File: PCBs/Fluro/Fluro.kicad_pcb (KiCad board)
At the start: 2 copper layers, 7 parts, among them J1 Conn_01x01_Pin, U1 OPT101P, U2 LM393N

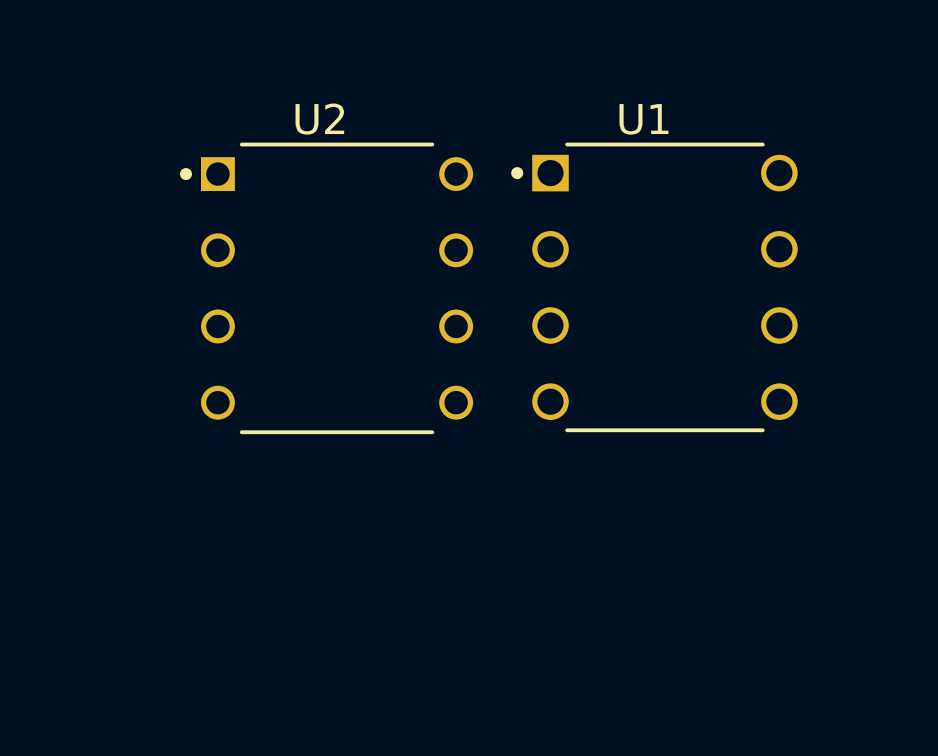
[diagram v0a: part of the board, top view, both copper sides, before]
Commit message: umdloop_swerve added
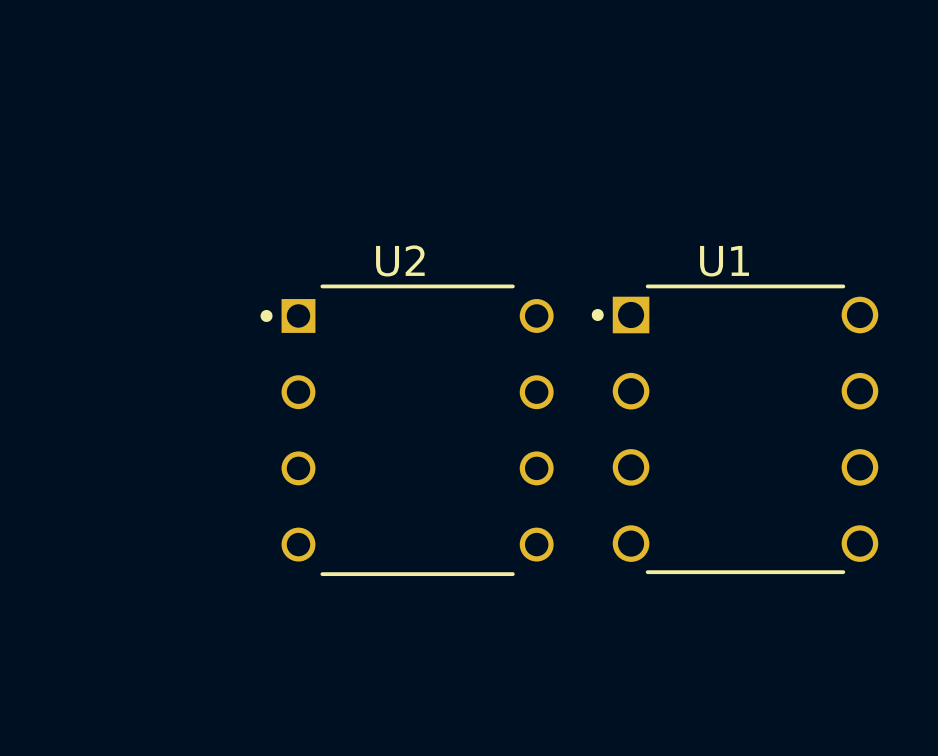
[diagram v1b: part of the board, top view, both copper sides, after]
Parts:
- moved U1 5.44 mm to (176.5, 72.0)
- moved U2 5.44 mm to (165.6, 72.0)
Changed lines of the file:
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@@
 	(footprint "LM393N_NOPB:DIP794W45P254L959H508Q8"
 		(layer "F.Cu")
-		(at 162.885 67.3025)
+		(at 165.57 72.0325)
 		(property "Reference" "U2"
 			(at -0.565 -5.607 0)
@@
 	(footprint "OPT101P:DIP762W46P254L952H419Q8"
 		(layer "F.Cu")
-		(at 173.815 67.27)
+		(at 176.5 72)
 		(property "Reference" "U1"
 			(at -0.695 -5.5745 0)
